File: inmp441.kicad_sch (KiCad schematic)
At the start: 5 parts

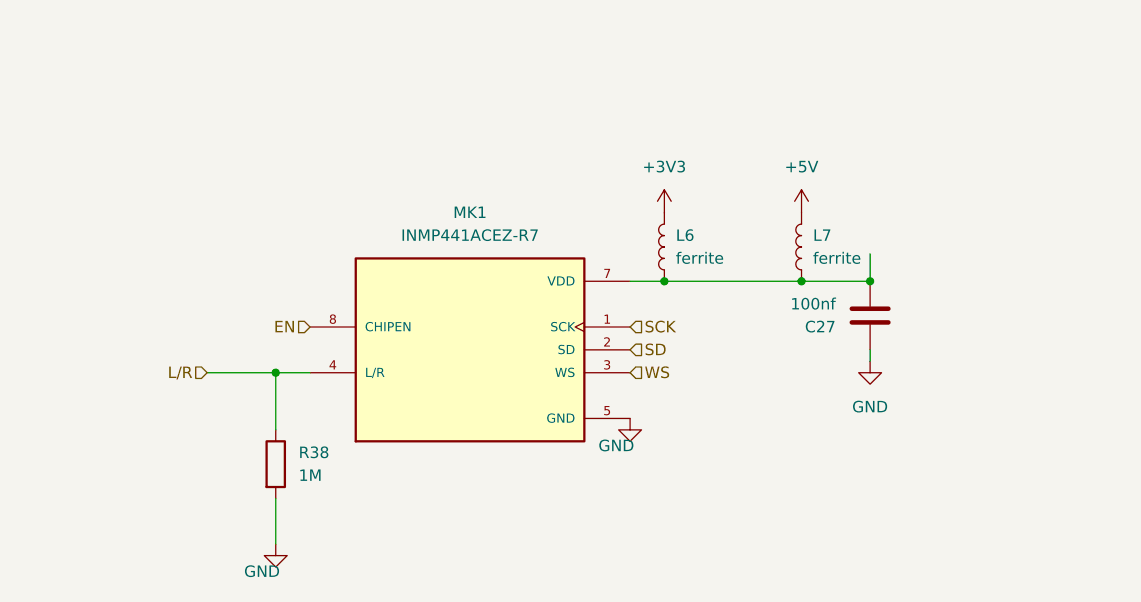
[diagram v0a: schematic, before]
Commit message: Actualización de esquemáticos y PCB
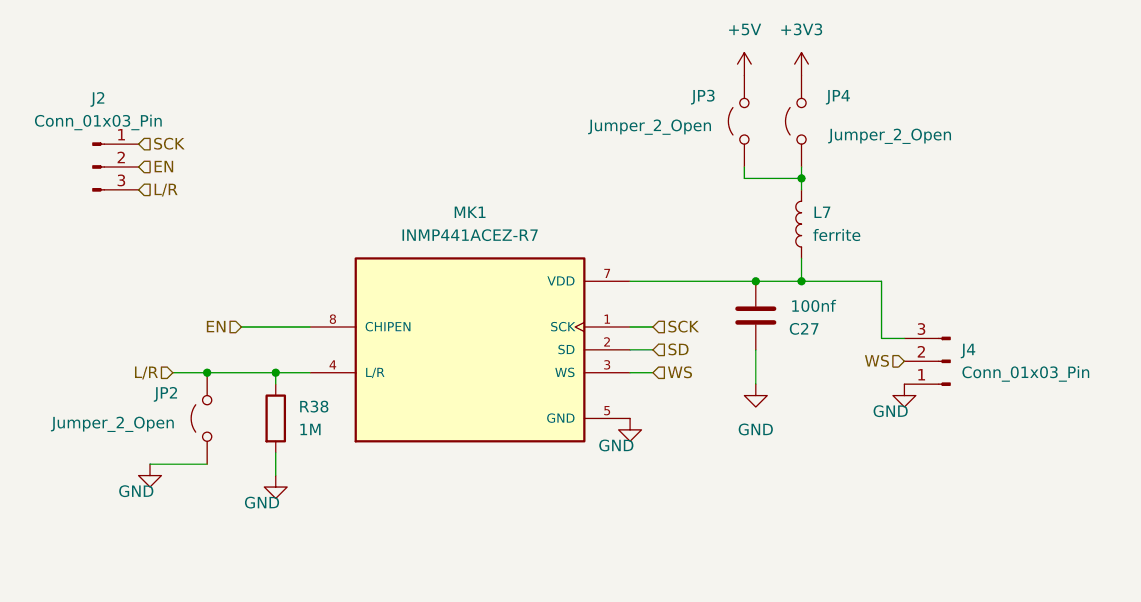
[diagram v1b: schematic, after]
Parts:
- removed L6: ferrite, Inductor_SMD:L_0805_2012Metric, symbol Device:L
- added J2, J4: Conn_01x03_Pin, Connector_PinHeader_2.54mm:PinHeader_1x03_P2.54mm_Vertical, symbol Connector:Conn_01x03_Pin
- added JP2: Jumper_2_Open, Jumper:SolderJumper-2_P1.3mm_Bridged_RoundedPad1.0x1.5mm, symbol Jumper:Jumper_2_Open
- added JP3, JP4: Jumper_2_Open, Jumper:SolderJumper-2_P1.3mm_Open_RoundedPad1.0x1.5mm, symbol Jumper:Jumper_2_Open
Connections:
- net +3V3: now also JP4.2 (B)
- net +5V: now also JP3.2 (B); no longer L7.2
- net EN: now also J2.2 (Pin_2)
- net GND: now also J4.1 (Pin_1), JP2.1 (A)
- net L/R: now also J2.3 (Pin_3), JP2.2 (B)
- net SCK: now also J2.1 (Pin_1)
- net WS: now also J4.2 (Pin_2)
- net at C27.2, L7.1, MK1.7 (VDD): now also J4.3 (Pin_3)
- new net: JP3.1 (A), JP4.1 (A), L7.2
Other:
- moved on the sheet: C27, L7, R38
